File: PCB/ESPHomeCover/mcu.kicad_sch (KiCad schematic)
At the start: 16 parts, among them IC1 ESP32-WROOM-32E-N4, SW1 SW_BOOT, SW2 SW_RESET, X3 I2C, X4 SPI, Y1 32.768KHz

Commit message: Add Board
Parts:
- C1: value 22uF -> 22uF 6.3V; footprint (none) -> Capacitor_SMD:C_0805_2012Metric; LCSC (none) -> C77071
- C2, C6: value 0.1uF -> 100nF 6.3V; footprint (none) -> Capacitor_SMD:C_0805_2012Metric; LCSC (none) -> C1854118
- C3: value 100nF -> 100nF 6.3V; footprint (none) -> Capacitor_SMD:C_0805_2012Metric; LCSC (none) -> C1854118
- C4, C5: value 12pF -> 12.5pF; footprint (none) -> Capacitor_SMD:C_0805_2012Metric
- J3: renamed from X3; footprint (none) -> Connector_JST:JST_XH_B4B-XH-A_1x04_P2.50mm_Vertical; now not fitted
- J4: renamed from X4; footprint (none) -> Connector_JST:JST_XH_B6B-XH-A_1x06_P2.50mm_Vertical; now not fitted
- R1: footprint (none) -> Resistor_SMD:R_0805_2012Metric; LCSC (none) -> C17414
- R2: footprint (none) -> Resistor_SMD:R_0805_2012Metric
- R3: value 10K -> 10k; footprint (none) -> Resistor_SMD:R_0805_2012Metric; LCSC (none) -> C17414
- X2: value ~ -> Prog Header
- Y1: footprint (none) -> Crystal:Crystal_SMD_2012-2Pin_2.0x1.2mm; LCSC (none) -> C5366544
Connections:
- net fault_motor: no longer IC1.26 (IO4)
- net CLK renamed SPI_CLK
- net CS renamed SPI_CS
- net MISO renamed SPI_MISO
- net MOSI renamed SPI_MOSI
- net SCL renamed I2C_SCL
- net SDA renamed I2C_SDA
- no-connect marks 3 -> 4
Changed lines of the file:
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@@
 	(title_block
 		(title "ESPHome Cover PCB")
-		(date "2024-05-07")
+		(date "2024-05-08")
 		(rev "1")
 	)
@@
 		(at 127 129.54)
 	)
+	(no_connect
+		(at 165.1 76.2)
+	)
 	(wire
 		(pts
@@
 		)
 	)
-	(label "SCL"
+	(label "I2C_SCL"
 		(at 194.31 118.11 0)
 		(fields_autoplaced yes)
@@
 		)
 	)
-	(label "fault_motor"
-		(at 165.1 76.2 0)
-		(fields_autoplaced yes)
-		(effects
-			(font
-				(size 1.27 1.27)
-			)
-			(justify left bottom)
-		)
-	)
 	(label "sen_down"
 		(at 45.72 49.53 180)
@@
 		)
 	)
-	(label "MISO"
+	(label "SPI_MISO"
 		(at 194.31 132.08 0)
 		(fields_autoplaced yes)
@@
 		)
 	)
-	(label "SCL"
+	(label "I2C_SCL"
 		(at 165.1 101.6 0)
 		(fields_autoplaced yes)
@@
 		)
 	)
-	(label "MISO"
+	(label "SPI_MISO"
 		(at 165.1 88.9 0)
 		(fields_autoplaced yes)
@@
 		)
 	)
-	(label "SDA"
+	(label "I2C_SDA"
 		(at 165.1 93.98 0)
 		(fields_autoplaced yes)
@@
 		)
 	)
-	(label "MOSI"
+	(label "SPI_MOSI"
 		(at 194.31 129.54 0)
 		(fields_autoplaced yes)
@@
 		)
 	)
-	(label "CS"
+	(label "SPI_CS"
 		(at 194.31 137.16 0)
 		(fields_autoplaced yes)
@@
 		)
 	)
-	(label "CLK"
+	(label "SPI_CLK"
 		(at 165.1 86.36 0)
 		(fields_autoplaced yes)
@@
 		)
 	)
-	(label "MOSI"
+	(label "SPI_MOSI"
 		(at 165.1 104.14 0)
 		(fields_autoplaced yes)
@@
 		)
 	)
-	(label "CLK"
+	(label "SPI_CLK"
 		(at 194.31 134.62 0)
 		(fields_autoplaced yes)
@@
 		)
 	)
-	(label "CS"
+	(label "SPI_CS"
 		(at 165.1 83.82 0)
 		(fields_autoplaced yes)
@@
 		)
 	)
-	(label "SDA"
+	(label "I2C_SDA"
 		(at 194.31 115.57 0)
 		(fields_autoplaced yes)
@@
 			)
 		)
-		(property "Value" "100nF"
+		(property "Value" "100nF 6.3V"
 			(at 107.95 94.742 90)
 			(effects
@@
 			)
 		)
-		(property "Footprint" ""
+		(property "Footprint" "Capacitor_SMD:C_0805_2012Metric"
 			(at 111.76 89.8652 0)
 			(effects
@@
 			)
 		)
+		(property "LCSC" "C1854118"
+			(at 107.95 88.9 0)
+			(effects
+				(font
+					(size 1.27 1.27)
+				)
+				(hide yes)
+			)
+		)
 		(pin "2"
 		)
@@
 		)
 		(property "Value" "5 MΩ ~ 10 MΩ"
-			(at 102.87 103.124 0)
+			(at 101.6 103.124 0)
 			(effects
 				(font
@@
 			)
 		)
-		(property "Footprint" ""
+		(property "Footprint" "Resistor_SMD:R_0805_2012Metric"
 			(at 95.758 101.6 90)
 			(effects
@@
 			)
 		)
-		(property "Value" "12pF"
+		(property "Value" "12.5pF"
 			(at 81.28 91.44 90)
 			(effects
@@
 			)
 		)
-		(property "Footprint" ""
+		(property "Footprint" "Capacitor_SMD:C_0805_2012Metric"
 			(at 85.09 95.5548 0)
 			(effects
@@
 		(in_bom yes)
 		(on_board yes)
-		(dnp no)
+		(dnp yes)
 		(fields_autoplaced yes)
-		(property "Reference" "X3"
+		(property "Reference" "J3"
 			(at 214.63 113.0299 0)
 			(effects
@@
 			)
 		)
-		(property "Footprint" ""
+		(property "Footprint" "Connector_JST:JST_XH_B4B-XH-A_1x04_P2.50mm_Vertical"
 			(at 212.09 113.03 0)
 			(effects
@@
 			(project "ESPHomeCover"
 				(path "/457ec9a0-69c6-4fbc-b0c1-e7e1db8d25f0/2f92e6c9-6e60-48cc-a739-61ad77952530"
-					(reference "X3")
+					(reference "J3")
 					(unit 1)
 				)
@@
 			)
 		)
-		(property "Value" "0.1uF"
+		(property "Value" "100nF 6.3V"
 			(at 119.38 73.6599 0)
 			(effects
@@
 			)
 		)
-		(property "Footprint" ""
+		(property "Footprint" "Capacitor_SMD:C_0805_2012Metric"
 			(at 116.5352 76.2 0)
 			(effects
@@
 			)
 		)
+		(property "LCSC" "C1854118"
+			(at 115.57 72.39 0)
+			(effects
+				(font
+					(size 1.27 1.27)
+				)
+				(hide yes)
+			)
+		)
 		(pin "1"
 		)
@@
 			)
 		)
-		(property "Value" "~"
+		(property "Value" "Prog Header"
 			(at 215.9 96.52 0)
 			(effects
@@
 			)
 		)
-		(property "Value" "10K"
+		(property "Value" "10k"
 			(at 181.61 84.074 90)
 			(effects
@@
 			)
 		)
-		(property "Footprint" ""
+		(property "Footprint" "Resistor_SMD:R_0805_2012Metric"
 			(at 181.61 80.518 90)
 			(effects
@@
 			)
 		)
+		(property "LCSC" "C17414"
+			(at 181.61 78.74 0)
+			(effects
+				(font
+					(size 1.27 1.27)
+				)
+				(hide yes)
+			)
+		)
 		(pin "1"
 		)
@@
 			)
 		)
-		(property "Value" "22uF"
+		(property "Value" "22uF 6.3V"
 			(at 106.68 73.6599 0)
 			(effects
@@
 			)
 		)
-		(property "Footprint" ""
+		(property "Footprint" "Capacitor_SMD:C_0805_2012Metric"
 			(at 103.8352 76.2 0)
 			(effects
@@
 			)
 		)
+		(property "LCSC" "C77071"
+			(at 102.87 72.39 0)
+			(effects
+				(font
+					(size 1.27 1.27)
+				)
+				(hide yes)
+			)
+		)
 		(pin "1"
 		)
@@
 		(in_bom yes)
 		(on_board yes)
-		(dnp no)
+		(dnp yes)
 		(fields_autoplaced yes)
-		(property "Reference" "X4"
+		(property "Reference" "J4"
 			(at 214.63 129.5399 0)
 			(effects
@@
 			)
 		)
-		(property "Footprint" ""
+		(property "Footprint" "Connector_JST:JST_XH_B6B-XH-A_1x06_P2.50mm_Vertical"
 			(at 212.09 129.54 0)
 			(effects
@@
 			(project "ESPHomeCover"
 				(path "/457ec9a0-69c6-4fbc-b0c1-e7e1db8d25f0/2f92e6c9-6e60-48cc-a739-61ad77952530"
-					(reference "X4")
+					(reference "J4")
 					(unit 1)
 				)
@@
 			)
 		)
-		(property "Value" "0.1uF"
+		(property "Value" "100nF 6.3V"
 			(at 239.776 59.69 90)
 			(effects
@@
 			)
 		)
-		(property "Footprint" ""
+		(property "Footprint" "Capacitor_SMD:C_0805_2012Metric"
 			(at 236.22 54.3052 0)
 			(effects
@@
 			)
 		)
+		(property "LCSC" "C1854118"
+			(at 240.03 53.34 0)
+			(effects
+				(font
+					(size 1.27 1.27)
+				)
+				(hide yes)
+			)
+		)
 		(pin "1"
 		)
@@
 			)
 		)
-		(property "Footprint" ""
+		(property "Footprint" "Resistor_SMD:R_0805_2012Metric"
 			(at 107.95 80.518 90)
 			(effects
@@
 			)
 		)
+		(property "LCSC" "C17414"
+			(at 107.95 78.74 0)
+			(effects
+				(font
+					(size 1.27 1.27)
+				)
+				(hide yes)
+			)
+		)
 		(pin "1"
 		)
@@
 			)
 		)
-		(property "Footprint" ""
+		(property "Footprint" "Crystal:Crystal_SMD_2012-2Pin_2.0x1.2mm"
 			(at 87.63 101.6 0)
 			(effects
@@
 			)
 		)
+		(property "LCSC" "C5366544"
+			(at 87.63 101.6 90)
+			(effects
+				(font
+					(size 1.27 1.27)
+				)
+				(hide yes)
+			)
+		)
 		(pin "2"
 		)
@@
 			)
 		)
-		(property "Value" "12pF"
+		(property "Value" "12.5pF"
 			(at 81.28 113.03 90)
 			(effects
@@
 			)
 		)
-		(property "Footprint" ""
+		(property "Footprint" "Capacitor_SMD:C_0805_2012Metric"
 			(at 85.09 105.7148 0)
 			(effects

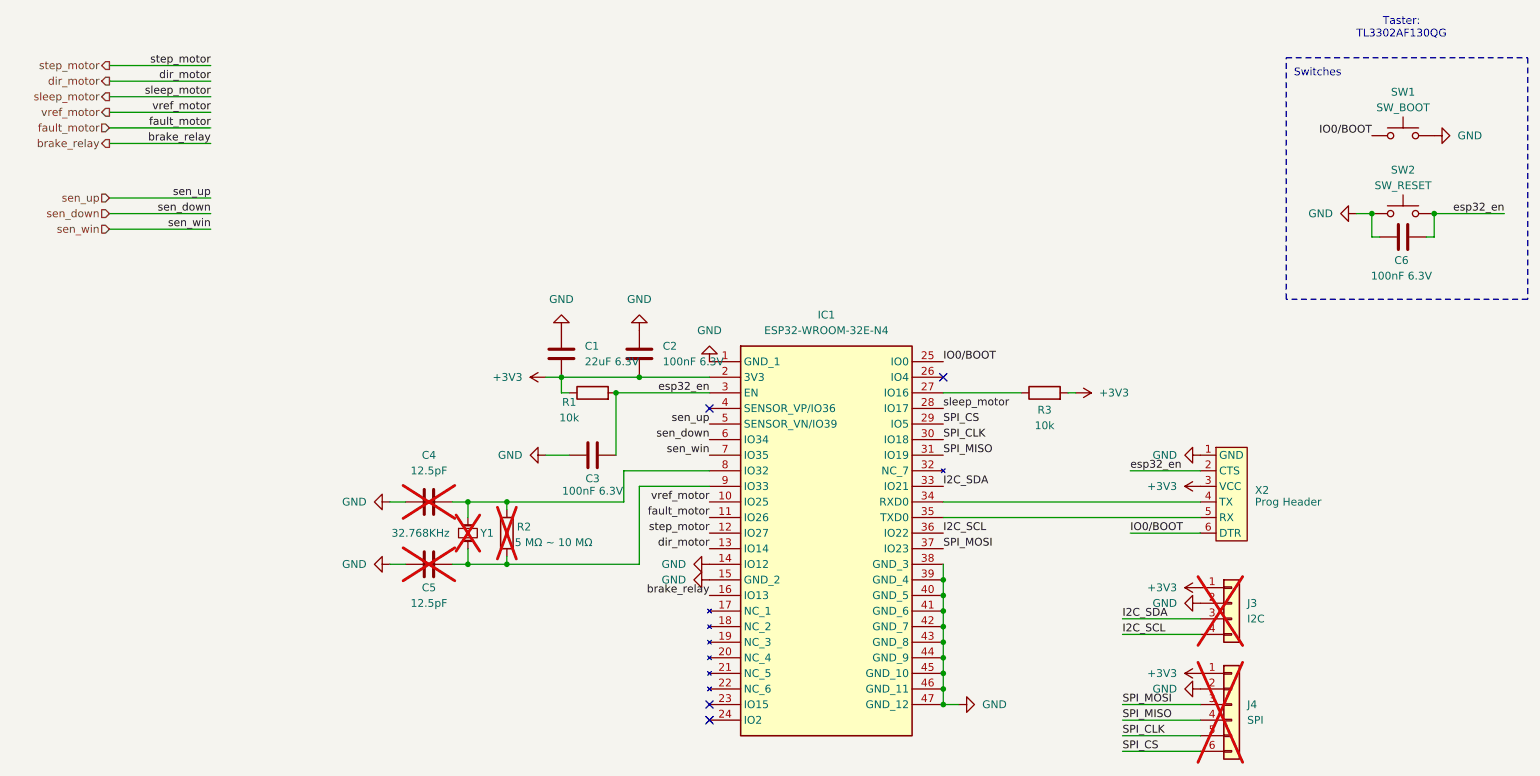
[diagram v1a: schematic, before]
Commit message: small changes
change all Caps to 0603,
add bom
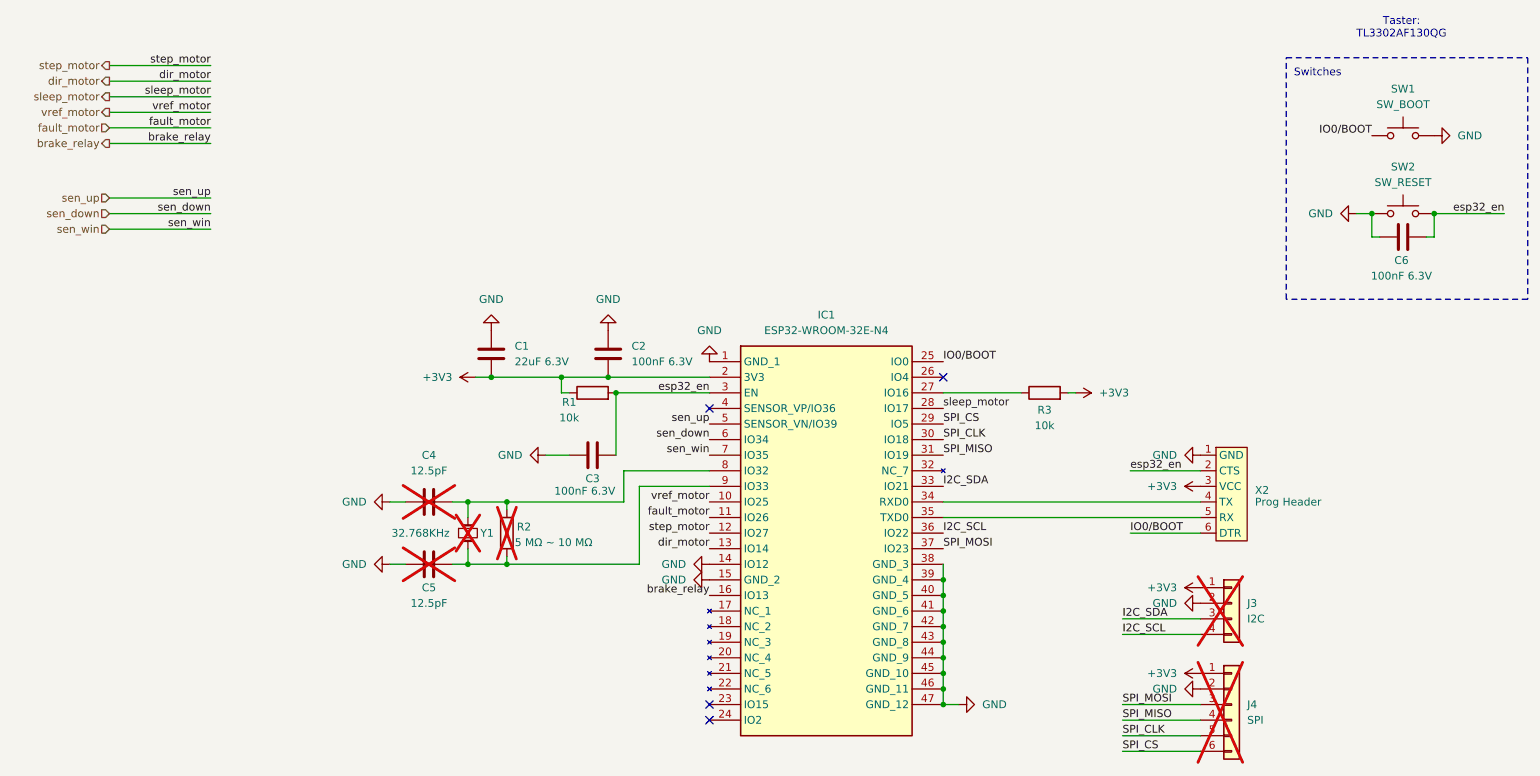
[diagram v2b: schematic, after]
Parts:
- removed SW1: SW_BOOT, symbol Switch:SW_Push
- removed SW2: SW_RESET, symbol Switch:SW_Push
- added SW1: SW_BOOT, SamacSys_Parts:TL3302AF130QG, symbol SamacSys_Parts:TL3302AF130QG
- added SW2: SW_RESET, SamacSys_Parts:TL3302AF130QG, symbol SamacSys_Parts:TL3302AF130QG
- C1: footprint Capacitor_SMD:C_0805_2012Metric -> Capacitor_SMD:C_0603_1608Metric; LCSC C77071 -> C159801
- C2, C3, C6: footprint Capacitor_SMD:C_0805_2012Metric -> Capacitor_SMD:C_0603_1608Metric; LCSC C1854118 -> (none)
- C4, C5: footprint Capacitor_SMD:C_0805_2012Metric -> Capacitor_SMD:C_0603_1608Metric
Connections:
- net GND: now also SW1.2, SW2.1
- net IO0/BOOT: now also SW1.1
- net esp32_en: now also SW2.2
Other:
- company: (none) -> Tim
- moved on the sheet: C1, C2

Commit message: update PCB
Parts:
- C1: Mouser Part Number (none) -> 963-MSASJ168BB5226MT
- C2, C3, C6: Mouser Part Number (none) -> 581-06036C104JAT2A
- J1: renamed from X2; now left out of the parts list
- R1, R3: Mouser Part Number (none) -> 667-ERA-6AEB103V
- renumbered J3 to J2, J4 to J3
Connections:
- net GND: now also C6.1; no longer C6.2
- net esp32_en: now also C6.2; no longer C6.1
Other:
- note removed: "Taster: TL3302AF130QG"
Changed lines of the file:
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@@
 		(title "ESPHome Cover PCB")
 		(date "2024-05-12")
-		(rev "2")
+		(rev "1")
 		(company "Tim")
 	)
@@
 	(wire
 		(pts
-			(xy 232.41 49.53) (xy 234.95 49.53)
+			(xy 247.65 49.53) (xy 245.11 49.53)
 		)
 		(stroke
@@
 	(wire
 		(pts
+			(xy 245.11 36.83) (xy 247.65 36.83)
+		)
+		(stroke
+			(width 0)
+			(type default)
+		)
+	)
+	(wire
+		(pts
+			(xy 223.52 36.83) (xy 234.95 36.83)
+		)
+		(stroke
+			(width 0)
+			(type default)
+		)
+	)
+	(wire
+		(pts
 			(xy 74.93 106.68) (xy 77.47 106.68)
 		)
@@
 	(wire
 		(pts
-			(xy 245.11 49.53) (xy 256.54 49.53)
+			(xy 234.95 49.53) (xy 223.52 49.53)
 		)
 		(stroke
@@
 		)
 	)
-	(text "Taster:\nTL3302AF130QG"
-		(exclude_from_sim no)
-		(at 239.776 19.304 0)
-		(effects
-			(font
-				(size 1.27 1.27)
-			)
-		)
-	)
 	(text "Switches"
 		(exclude_from_sim no)
@@
 	)
 	(label "IO0{slash}BOOT"
-		(at 234.95 36.83 180)
+		(at 223.52 36.83 0)
 		(fields_autoplaced yes)
 		(effects
@@
 				(size 1.27 1.27)
 			)
-			(justify right bottom)
+			(justify left bottom)
 		)
 	)
@@
 	)
 	(label "esp32_en"
-		(at 256.54 49.53 180)
+		(at 223.52 49.53 0)
 		(fields_autoplaced yes)
 		(effects
@@
 				(size 1.27 1.27)
 			)
-			(justify right bottom)
+			(justify left bottom)
 		)
 	)
@@
 			)
 		)
+		(property "Mouser Part Number" "581-06036C104JAT2A"
+			(at 107.95 88.9 0)
+			(effects
+				(font
+					(size 1.27 1.27)
+				)
+				(hide yes)
+			)
+		)
 		(pin "2"
 		)
@@
 		(dnp yes)
 		(fields_autoplaced yes)
-		(property "Reference" "J3"
+		(property "Reference" "J2"
 			(at 214.63 113.0299 0)
 			(effects
@@
 			(project "ESPHomeCover"
 				(path "/457ec9a0-69c6-4fbc-b0c1-e7e1db8d25f0/2f92e6c9-6e60-48cc-a739-61ad77952530"
-					(reference "J3")
+					(reference "J2")
 					(unit 1)
 				)
@@
 			)
 		)
+		(property "Mouser Part Number" "581-06036C104JAT2A"
+			(at 110.49 72.39 0)
+			(effects
+				(font
+					(size 1.27 1.27)
+				)
+				(hide yes)
+			)
+		)
 		(pin "1"
 		)
@@
 		(unit 1)
 		(exclude_from_sim no)
-		(in_bom yes)
+		(in_bom no)
 		(on_board yes)
 		(dnp no)
 		(fields_autoplaced yes)
-		(property "Reference" "X2"
-			(at 215.9 94.6149 0)
+		(property "Reference" "J1"
+			(at 215.9 93.9799 0)
 			(effects
 				(font
@@
 		)
 		(property "Value" "Prog Header"
-			(at 215.9 96.52 0)
+			(at 215.9 96.5199 0)
 			(effects
 				(font
@@
 			(project "ESPHomeCover"
 				(path "/457ec9a0-69c6-4fbc-b0c1-e7e1db8d25f0/2f92e6c9-6e60-48cc-a739-61ad77952530"
-					(reference "X2")
+					(reference "J1")
 					(unit 1)
 				)
@@
 			)
 		)
+		(property "Mouser Part Number" "667-ERA-6AEB103V"
+			(at 181.61 78.74 0)
+			(effects
+				(font
+					(size 1.27 1.27)
+				)
+				(hide yes)
+			)
+		)
 		(pin "1"
 		)
@@
 			)
 		)
+		(property "Mouser Part Number" "963-MSASJ168BB5226MT"
+			(at 91.44 72.39 0)
+			(effects
+				(font
+					(size 1.27 1.27)
+				)
+				(hide yes)
+			)
+		)
 		(pin "1"
 		)
@@
 		(dnp yes)
 		(fields_autoplaced yes)
-		(property "Reference" "J4"
+		(property "Reference" "J3"
 			(at 214.63 129.5399 0)
 			(effects
@@
 			(project "ESPHomeCover"
 				(path "/457ec9a0-69c6-4fbc-b0c1-e7e1db8d25f0/2f92e6c9-6e60-48cc-a739-61ad77952530"
-					(reference "J4")
+					(reference "J3")
 					(unit 1)
 				)
@@
 			)
 		)
+		(property "Mouser Part Number" "581-06036C104JAT2A"
+			(at 240.03 53.34 0)
+			(effects
+				(font
+					(size 1.27 1.27)
+				)
+				(hide yes)
+			)
+		)
 		(pin "1"
 		)
@@
 	(symbol
 		(lib_id "power:GND")
-		(at 245.11 36.83 90)
+		(at 247.65 36.83 90)
 		(unit 1)
 		(exclude_from_sim no)
@@
 		(fields_autoplaced yes)
 		(property "Reference" "#PWR020"
-			(at 251.46 36.83 0)
+			(at 254 36.83 0)
 			(effects
 				(font
@@
 		)
 		(property "Value" "GND"
-			(at 248.92 36.8299 90)
+			(at 251.46 36.8299 90)
 			(effects
 				(font
@@
 		)
 		(property "Footprint" ""
-			(at 245.11 36.83 0)
+			(at 247.65 36.83 0)
 			(effects
 				(font
@@
 		)
 		(property "Datasheet" ""
-			(at 245.11 36.83 0)
+			(at 247.65 36.83 0)
 			(effects
 				(font
@@
 		)
 		(property "Description" "Power symbol creates a global label with name \"GND\" , ground"
-			(at 245.11 36.83 0)
+			(at 247.65 36.83 0)
 			(effects
 				(font
@@
 			)
 		)
+		(property "Mouser Part Number" "667-ERA-6AEB103V"
+			(at 107.95 78.74 0)
+			(effects
+				(font
+					(size 1.27 1.27)
+				)
+				(hide yes)
+			)
+		)
 		(pin "1"
 		)
@@
 	(symbol
 		(lib_id "power:GND")
-		(at 232.41 49.53 270)
+		(at 247.65 49.53 90)
+		(mirror x)
 		(unit 1)
 		(exclude_from_sim no)
@@
 		(fields_autoplaced yes)
 		(property "Reference" "#PWR025"
-			(at 226.06 49.53 0)
+			(at 254 49.53 0)
 			(effects
 				(font
@@
 		)
 		(property "Value" "GND"
-			(at 228.6 49.5299 90)
+			(at 251.46 49.5299 90)
 			(effects
 				(font
@@
 		)
 		(property "Footprint" ""
-			(at 232.41 49.53 0)
+			(at 247.65 49.53 0)
 			(effects
 				(font
@@
 		)
 		(property "Datasheet" ""
-			(at 232.41 49.53 0)
+			(at 247.65 49.53 0)
 			(effects
 				(font
@@
 		)
 		(property "Description" "Power symbol creates a global label with name \"GND\" , ground"
-			(at 232.41 49.53 0)
+			(at 247.65 49.53 0)
 			(effects
 				(font
@@
 		(lib_id "SamacSys_Parts:TL3302AF130QG")
 		(at 240.03 49.53 0)
+		(mirror y)
 		(unit 1)
 		(exclude_from_sim no)
@@
 		)
 		(property "Footprint" "SamacSys_Parts:TL3302AF130QG"
-			(at 259.08 144.45 0)
+			(at 220.98 144.45 0)
 			(effects
 				(font
@@
 		)
 		(property "Datasheet" "https://configured-product-images.s3.amazonaws.com/2D/specs/TL3302AF130QG.pdf"
-			(at 259.08 244.45 0)
+			(at 220.98 244.45 0)
 			(effects
 				(font
@@
 		)
 		(property "Height" "4.55"
-			(at 259.08 444.45 0)
+			(at 220.98 444.45 0)
 			(effects
 				(font
@@
 		)
 		(property "Mouser Part Number" "612-TL3302AF130QG"
-			(at 259.08 544.45 0)
+			(at 220.98 544.45 0)
 			(effects
 				(font
@@
 		)
 		(property "Mouser Price/Stock" "https://www.mouser.co.uk/ProductDetail/E-Switch/TL3302AF130QG?qs=QtyuwXswaQjypAFh0ff2%2FQ%3D%3D"
-			(at 259.08 644.45 0)
+			(at 220.98 644.45 0)
 			(effects
 				(font
@@
 		)
 		(property "Manufacturer_Name" "E-Switch"
-			(at 259.08 744.45 0)
+			(at 220.98 744.45 0)
 			(effects
 				(font
@@
 		)
 		(property "Manufacturer_Part_Number" "TL3302AF130QG"
-			(at 259.08 844.45 0)
+			(at 220.98 844.45 0)
 			(effects
 				(font

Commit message: update PCB
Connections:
- net GND: now also IC1.24 (IO2)
- no-connect marks 4 -> 3
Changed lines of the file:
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@@
 	(title_block
 		(title "ESPHome Cover PCB")
-		(date "2024-05-12")
+		(date "2024-05-27")
 		(rev "1")
 		(company "Tim")
@@
 		(diameter 0)
 		(color 0 0 0 0)
-	)
-	(no_connect
-		(at 127 132.08)
 	)
 	(no_connect
@@
 		)
 	)
+	(symbol
+		(lib_id "power:GND")
+		(at 127 132.08 270)
+		(unit 1)
+		(exclude_from_sim no)
+		(in_bom yes)
+		(on_board yes)
+		(dnp no)
+		(fields_autoplaced yes)
+		(property "Reference" "#PWR062"
+			(at 120.65 132.08 0)
+			(effects
+				(font
+					(size 1.27 1.27)
+				)
+				(hide yes)
+			)
+		)
+		(property "Value" "GND"
+			(at 123.19 132.0799 90)
+			(effects
+				(font
+					(size 1.27 1.27)
+				)
+				(justify right)
+			)
+		)
+		(property "Footprint" ""
+			(at 127 132.08 0)
+			(effects
+				(font
+					(size 1.27 1.27)
+				)
+				(hide yes)
+			)
+		)
+		(property "Datasheet" ""
+			(at 127 132.08 0)
+			(effects
+				(font
+					(size 1.27 1.27)
+				)
+				(hide yes)
+			)
+		)
+		(property "Description" "Power symbol creates a global label with name \"GND\" , ground"
+			(at 127 132.08 0)
+			(effects
+				(font
+					(size 1.27 1.27)
+				)
+				(hide yes)
+			)
+		)
+		(pin "1"
+		)
+		(instances
+			(project "ESPHomeCover"
+				(path "/457ec9a0-69c6-4fbc-b0c1-e7e1db8d25f0/2f92e6c9-6e60-48cc-a739-61ad77952530"
+					(reference "#PWR062")
+					(unit 1)
+				)
+			)
+		)
+	)
